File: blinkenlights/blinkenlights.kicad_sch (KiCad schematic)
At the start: 23 parts, among them SW101 Black, SW102 Orang, SW103 SW_DIP_x01, U101 ATF22V10C, U102 SST39SF020, U103 SST39SF020, U104 74AUC2G07, U105 74AUC2G07, U106 74HC2G14

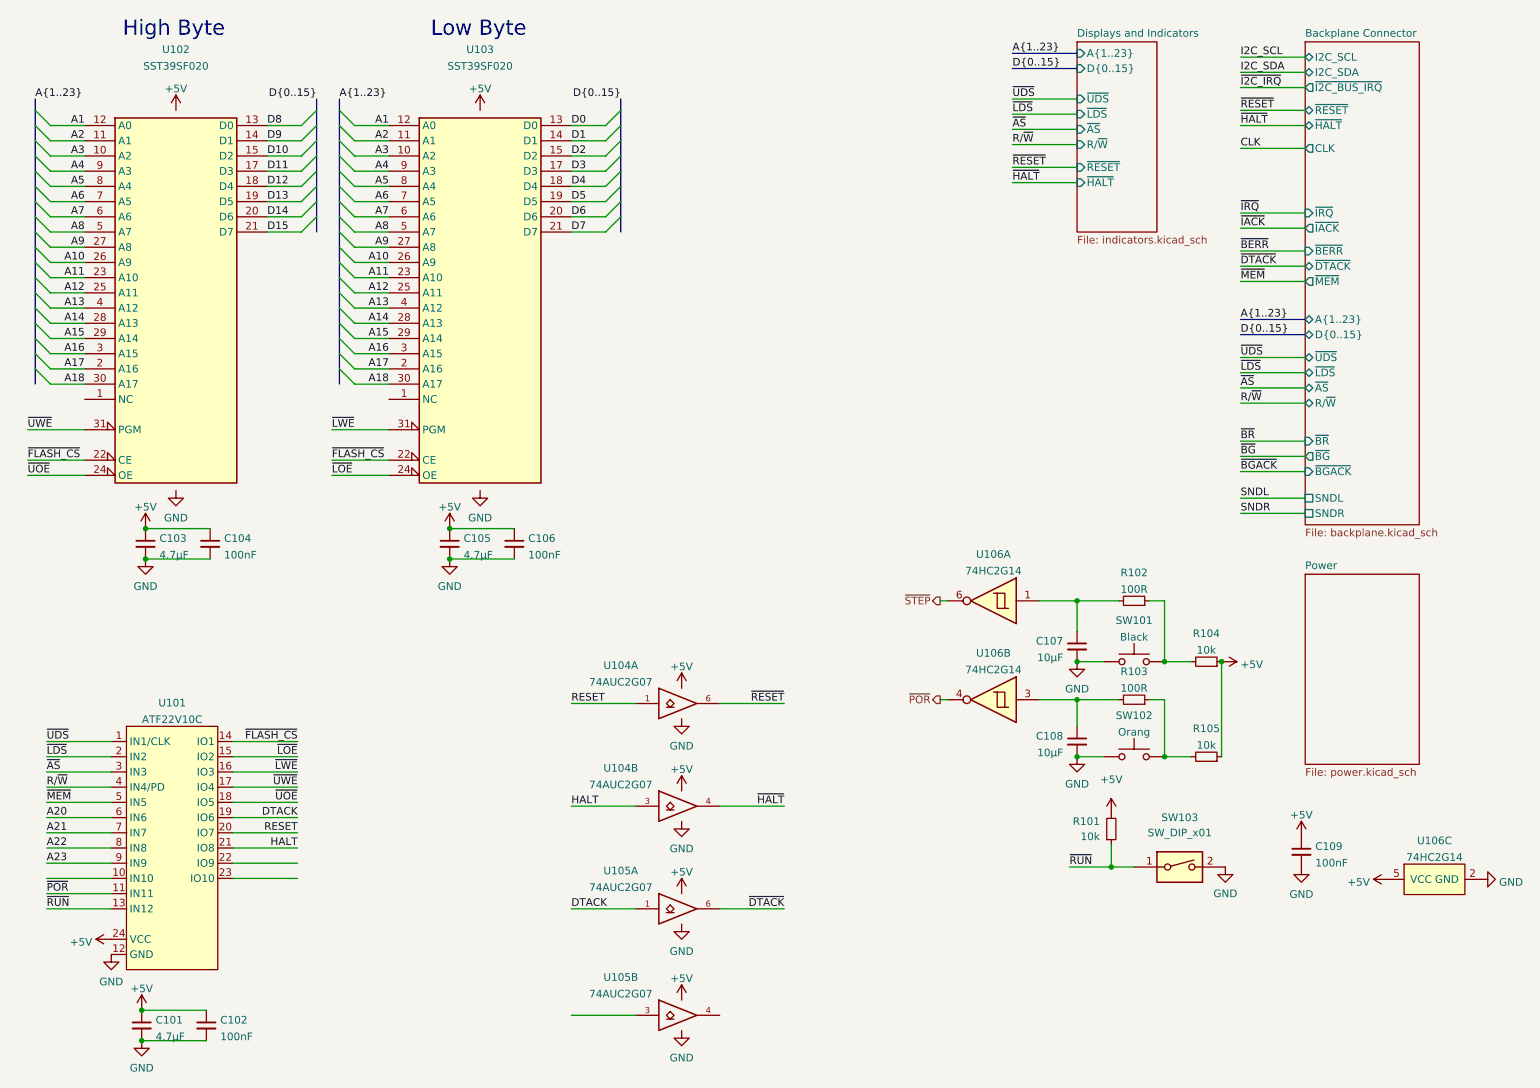
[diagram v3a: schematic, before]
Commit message: Rework blinkenlights board
- Removed ROMs, GALs and so forth from the blinkenlights board and
  simplified the power distribution significantly. This is in
  preparation for simply placing a big ass microcontroller that allows
  us to perform bus transactions manually (to load bootstrap programs,
  for example) on the system.
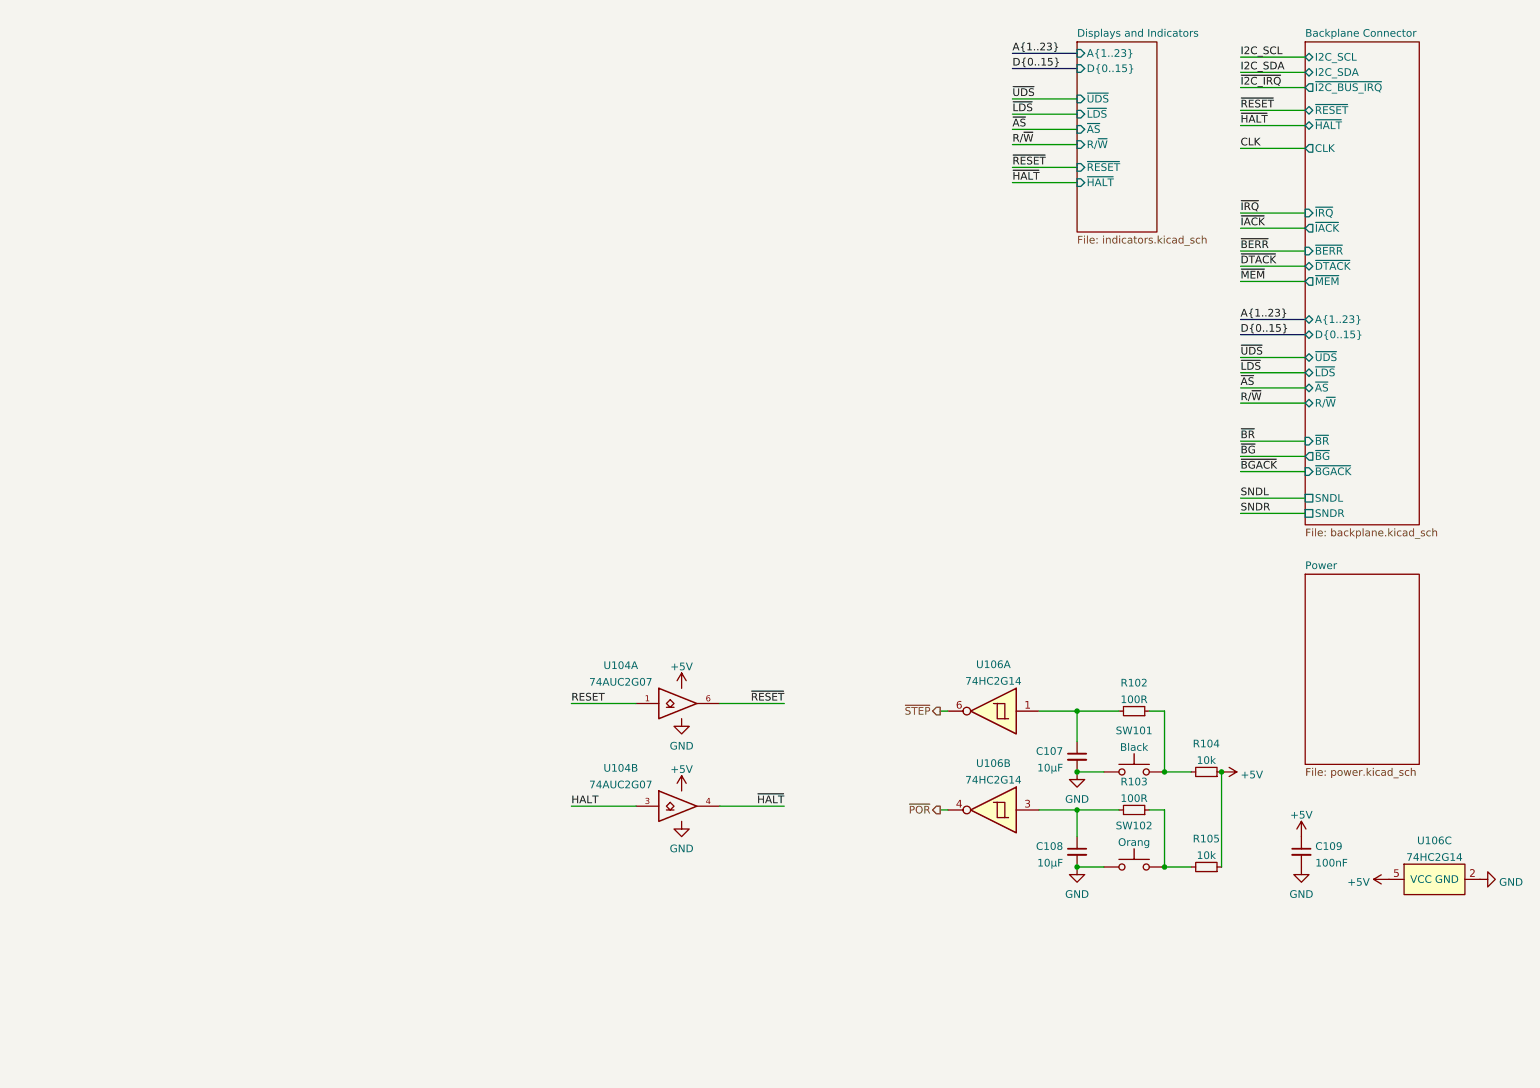
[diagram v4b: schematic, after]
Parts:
- removed C101, C103, C105: 4.7µF, Capacitor_SMD:C_0805_2012Metric, symbol Device:C_Small
- removed C102, C104, C106: 100nF, Capacitor_SMD:C_0805_2012Metric, symbol Device:C_Small
- removed R101: 10k, Resistor_SMD:R_0805_2012Metric, symbol Device:R_Small
- removed SW103: SW_DIP_x01, Button_Switch_THT:SW_DIP_SPSTx01_Slide_9.78x4.72mm_W7.62mm_P2.54mm, symbol Switch:SW_DIP_x01
- removed U101: ATF22V10C, Package_DIP:DIP-24_W7.62mm_Socket, symbol 68komputer-common:ATF22V10C
- removed U102, U103: SST39SF020, Socket:DIP_Socket-32_W11.9_W12.7_W15.24_W17.78_W18.5_3M_232-1285-00-0602J, symbol Memory_Flash:SST39SF020
- removed U105: 74AUC2G07, Package_TO_SOT_SMD:SOT-23-6, symbol 74xGxx:74AUC2G07
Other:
- note removed: "High Byte"
- note removed: "Low Byte"
- moved on the sheet: C107, C108, R102, R103, R104, R105, SW101, SW102, U106A, U106B

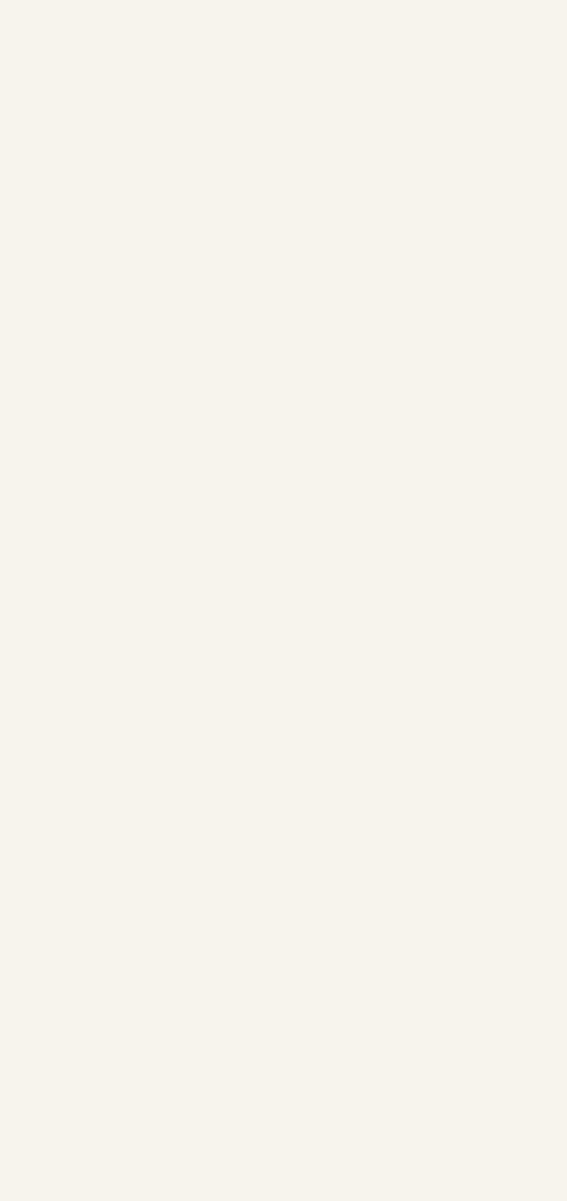
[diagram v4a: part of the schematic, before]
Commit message: Added ATSAM4 CPU to blinkenlights
- This big ol ARM chip is gonna be hooked up to the 68k bus, so that we
  can do bus transactions and (slowly) single step the physical machine.
  This will make bringup simpler and allow programming of the flash
  chips on the CPU board.

- Added a footprint for an USB-C connector (lol)
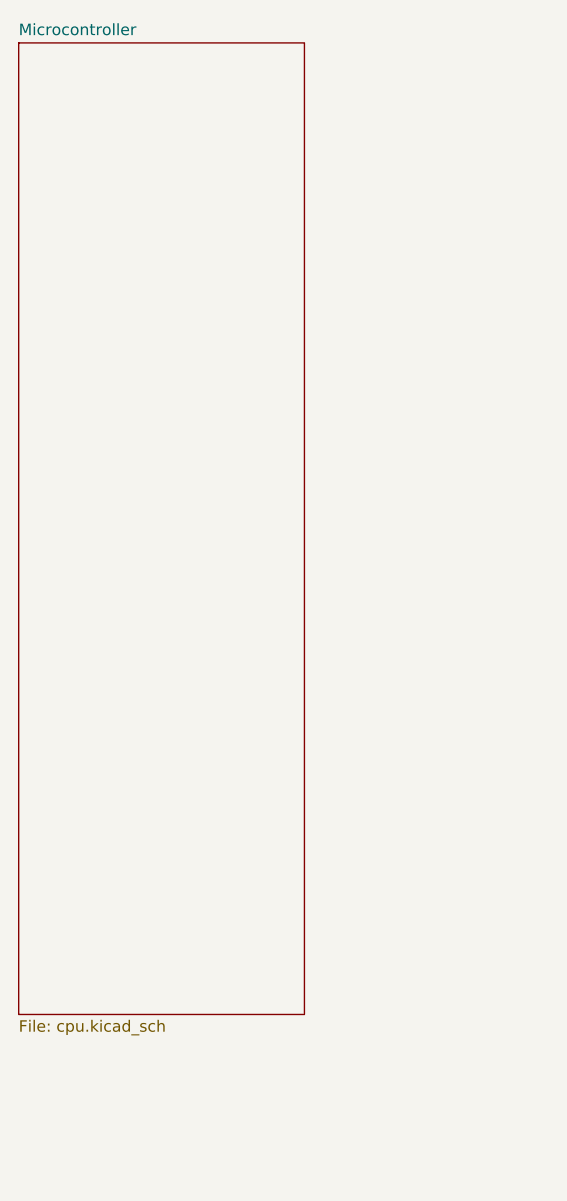
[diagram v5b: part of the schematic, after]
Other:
- added sheet Microcontroller (cpu.kicad_sch)

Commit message: Routed address/data bus on blinkenlights
- It goes to the funky hex display bois now and is routed so that it
  should be pretty ez to yeet on down into level shifters for the big
  ARM chip that runs the show
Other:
- sheet Backplane Connector ports: added A[1..23], D[0..15]; removed A{1..23}, D{0..15}
- sheet Displays and Indicators ports: added A[1..23], D[0..15]; removed A{1..23}, D{0..15}
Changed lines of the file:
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@@
+    (effects (font (size 1.27 1.27)) (justify left bottom))
+  )
+  (label "D[0..15]" (at 186.055 23.495 0)
     (effects (font (size 1.27 1.27)) (justify left bottom))
   )
@@
     (effects (font (size 1.27 1.27)) (justify left bottom))
   )
-  (label "D{0..15}" (at 186.055 23.495 0)
-    (effects (font (size 1.27 1.27)) (justify left bottom))
-  )
   (label "R{slash}~{W}" (at 186.055 36.195 0)
     (effects (font (size 1.27 1.27)) (justify left bottom))
   )
+  (label "A[1..23]" (at 186.055 20.955 0)
+    (effects (font (size 1.27 1.27)) (justify left bottom))
+  )
   (label "~{MEM}" (at 224.155 59.055 0)
     (effects (font (size 1.27 1.27)) (justify left bottom))
@@
     (effects (font (size 1.27 1.27)) (justify left bottom))
   )
-  (label "A{1..23}" (at 224.155 65.405 0)
-    (effects (font (size 1.27 1.27)) (justify left bottom))
-  )
-  (label "A{1..23}" (at 186.055 20.955 0)
+  (label "A[1..23]" (at 224.155 65.405 0)
     (effects (font (size 1.27 1.27)) (justify left bottom))
   )
@@
     (effects (font (size 1.27 1.27)) (justify left bottom))
   )
-  (label "D{0..15}" (at 224.155 67.945 0)
+  (label "D[0..15]" (at 224.155 67.945 0)
     (effects (font (size 1.27 1.27)) (justify left bottom))
   )
@@
       (effects (font (size 1.27 1.27)) (justify left top))
     )
-    (pin "A{1..23}" input (at 196.85 20.955 180)
-      (effects (font (size 1.27 1.27)) (justify left))
-    )
-    (pin "D{0..15}" input (at 196.85 23.495 180)
+    (pin "A[1..23]" input (at 196.85 20.955 180)
+      (effects (font (size 1.27 1.27)) (justify left))
+    )
+    (pin "D[0..15]" input (at 196.85 23.495 180)
       (effects (font (size 1.27 1.27)) (justify left))
     )
@@
       (effects (font (size 1.27 1.27)) (justify left))
     )
-    (pin "D{0..15}" bidirectional (at 234.95 67.945 180)
+    (pin "D[0..15]" bidirectional (at 234.95 67.945 180)
       (effects (font (size 1.27 1.27)) (justify left))
     )
@@
       (effects (font (size 1.27 1.27)) (justify left))
     )
-    (pin "A{1..23}" bidirectional (at 234.95 65.405 180)
+    (pin "A[1..23]" bidirectional (at 234.95 65.405 180)
       (effects (font (size 1.27 1.27)) (justify left))
     )
@@
       (reference "#PWR0505") (unit 1) (value "+3V3") (footprint "")
     )
+    (path "/69ba85f7-748f-4efd-b6fb-efc1542049b1/cd9dbe8a-6e02-485e-bb92-264485524ca1"
+      (reference "#PWR0506") (unit 1) (value "+3V3") (footprint "")
+    )
+    (path "/69ba85f7-748f-4efd-b6fb-efc1542049b1/c207d57d-6fb5-4904-bf8a-8f74e723abf0"
+      (reference "#PWR0507") (unit 1) (value "GND") (footprint "")
+    )
+    (path "/69ba85f7-748f-4efd-b6fb-efc1542049b1/9f86e0e8-a768-4c6f-adef-66625c204fa3"
+      (reference "#PWR0508") (unit 1) (value "GND") (footprint "")
+    )
+    (path "/69ba85f7-748f-4efd-b6fb-efc1542049b1/993d4deb-f3bd-4daf-a633-6a6f3f8cbf09"
+      (reference "#PWR0509") (unit 1) (value "GND") (footprint "")
+    )
+    (path "/69ba85f7-748f-4efd-b6fb-efc1542049b1/487af8a0-5496-4a08-a355-98e2cd265414"
+      (reference "#PWR0510") (unit 1) (value "+3V3") (footprint "")
+    )
+    (path "/69ba85f7-748f-4efd-b6fb-efc1542049b1/c74c6715-3746-4876-95da-9f8d9bc885c1"
+      (reference "#PWR0511") (unit 1) (value "GND") (footprint "")
+    )
+    (path "/69ba85f7-748f-4efd-b6fb-efc1542049b1/4a290f51-e0ff-49b7-a116-d4f87929a40b"
+      (reference "#PWR0512") (unit 1) (value "GND") (footprint "")
+    )
     (path "/69ba85f7-748f-4efd-b6fb-efc1542049b1/496cefc4-8de7-4537-93ea-320c76488292/2e57998d-121c-41e9-bbaa-6e63f9930929"
       (reference "#PWR0601") (unit 1) (value "+3V3") (footprint "")
@@
       (reference "C504") (unit 1) (value "100nF") (footprint "Capacitor_SMD:C_0805_2012Metric")
     )
+    (path "/69ba85f7-748f-4efd-b6fb-efc1542049b1/06729a9b-4220-4eaa-8fb0-1b8566eb5cbc"
+      (reference "C505") (unit 1) (value "100nF") (footprint "Capacitor_SMD:C_0805_2012Metric")
+    )
+    (path "/69ba85f7-748f-4efd-b6fb-efc1542049b1/22ef8ee7-aca5-48a8-98fa-38f2e38def0d"
+      (reference "C506") (unit 1) (value "100nF") (footprint "Capacitor_SMD:C_0805_2012Metric")
+    )
+    (path "/69ba85f7-748f-4efd-b6fb-efc1542049b1/414627c1-850d-4d0a-b9ce-9c564c0ec29f"
+      (reference "C507") (unit 1) (value "100nF") (footprint "Capacitor_SMD:C_0805_2012Metric")
+    )
+    (path "/69ba85f7-748f-4efd-b6fb-efc1542049b1/1e3eae80-d9ae-4b80-92c9-ba83fd2a21e8"
+      (reference "C508") (unit 1) (value "4.7µF") (footprint "Capacitor_SMD:C_0805_2012Metric")
+    )
+    (path "/69ba85f7-748f-4efd-b6fb-efc1542049b1/0ab9b269-f8f3-476c-acff-ee3d0f5de54d"
+      (reference "C509") (unit 1) (value "4.7µF") (footprint "Capacitor_SMD:C_0805_2012Metric")
+    )
+    (path "/69ba85f7-748f-4efd-b6fb-efc1542049b1/b61cb706-c2a0-4bd1-94f0-a52885a00f8e"
+      (reference "C510") (unit 1) (value "100nF") (footprint "Capacitor_SMD:C_0805_2012Metric")
+    )
+    (path "/69ba85f7-748f-4efd-b6fb-efc1542049b1/426ae12b-4d62-4876-802e-1adb6c8a99ea"
+      (reference "C511") (unit 1) (value "100nF") (footprint "Capacitor_SMD:C_0805_2012Metric")
+    )
+    (path "/69ba85f7-748f-4efd-b6fb-efc1542049b1/32b8a325-2cb1-4e0b-9542-5e0b2c7cb7a4"
+      (reference "C512") (unit 1) (value "4.7µF") (footprint "Capacitor_SMD:C_0805_2012Metric")
+    )
+    (path "/69ba85f7-748f-4efd-b6fb-efc1542049b1/d7b94ddb-be34-430f-a4d9-1efc5f3c326f"
+      (reference "C513") (unit 1) (value "10µF") (footprint "Capacitor_Tantalum_SMD:CP_EIA-3528-21_Kemet-B")
+    )
     (path "/69ba85f7-748f-4efd-b6fb-efc1542049b1/496cefc4-8de7-4537-93ea-320c76488292/59b0f73c-e494-458d-a990-cdda4c47ad8c"
       (reference "C601") (unit 1) (value "100nF") (footprint "Capacitor_SMD:C_0805_2012Metric")
@@
       (reference "L302") (unit 1) (value "4.7µH") (footprint "Inductor_SMD:L_Taiyo-Yuden_NR-80xx_HandSoldering")
     )
+    (path "/69ba85f7-748f-4efd-b6fb-efc1542049b1/a8563c98-faad-4464-a335-f62beab26c94"
+      (reference "L501") (unit 1) (value "10µH") (footprint "Inductor_SMD:L_0805_2012Metric")
+    )
     (path "/baeace01-fb99-44e2-89d5-88b5f21838a1"
       (reference "R102") (unit 1) (value "100R") (footprint "Resistor_SMD:R_0805_2012Metric")
@@
       (reference "R503") (unit 1) (value "10k") (footprint "Resistor_SMD:R_0805_2012Metric")
     )
+    (path "/69ba85f7-748f-4efd-b6fb-efc1542049b1/d6f17292-9b97-4f13-b507-7396695cf2e1"
+      (reference "R504") (unit 1) (value "1R") (footprint "Resistor_SMD:R_0805_2012Metric")
+    )
     (path "/69ba85f7-748f-4efd-b6fb-efc1542049b1/496cefc4-8de7-4537-93ea-320c76488292/a03396a2-cda6-4731-93bb-74201c0661ac"

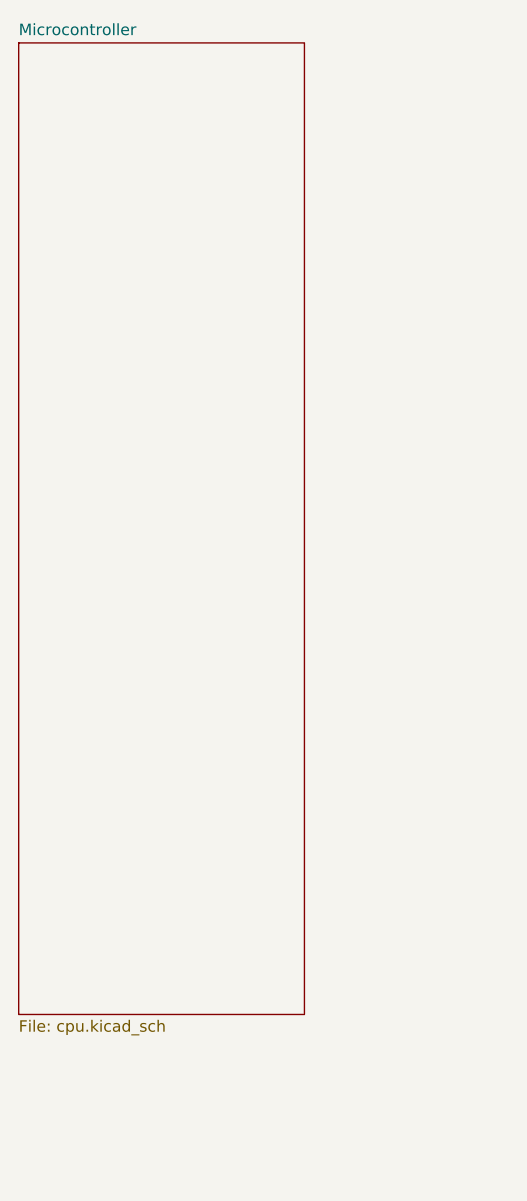
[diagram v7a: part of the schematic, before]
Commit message: Get rid of CPU on blinkenlights board
- We don't really care for having a full processor chilling on this
  board more than we do about being able to do a few bus transactions
  (to do fun stuff like flashing the boot ROMs) so we're going to put a
  bunch of SPI IO expanders instead; this should allow us to somewhat
  recreate bus cycles.

  We'll have to implement the run/halt/single step controls with
  dedicated logic though.
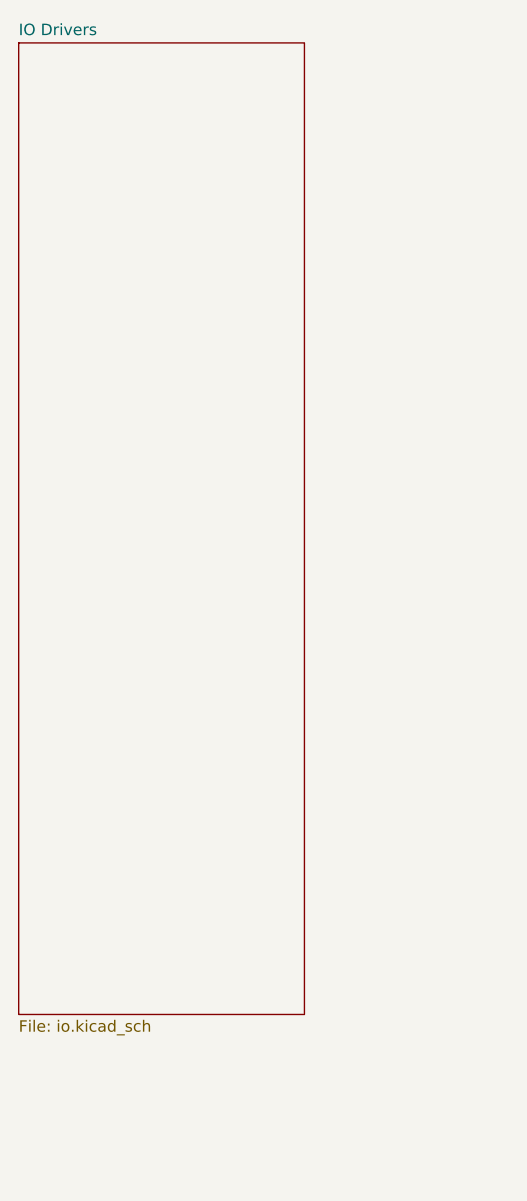
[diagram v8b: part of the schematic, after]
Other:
- sheet Microcontroller renamed IO Drivers
- sheet IO Drivers: file cpu.kicad_sch -> io.kicad_sch
